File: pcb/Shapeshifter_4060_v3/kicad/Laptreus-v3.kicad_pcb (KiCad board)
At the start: 2 copper layers, 285 x 94.6 mm, 107 parts, among them SW1 TAB, SW10 O, SW11 P, SW12 BKSP, SW13 ESC, SW14 A, SW15 S, SW16 D, SW17 F/LOWER, SW18 G, SW19 H, SW2 Q, SW20 J/RAISE, SW21 K, SW22 L, SW23 ;, SW24 ", SW25 SHIFT, SW26 Z, SW27 X, SW28 C, SW29 V, SW3 W, SW30 B, SW31 N, SW32 M, SW33 ,, SW34 ., SW35 /, SW36 ENTER, SW37 HYPER, SW38 CTRL/GRV, SW39 ALT/TAB, SW4 E, SW40 CMD, SW41 SHIFT, SW42 BKSP/LIFT, SW43 ENTER/LIFT, SW44 SPACE, SW45 LEFT, SW46 DOWN, SW47 UP, SW48 RIGHT, SW5 R, SW6 T, SW7 Y, SW8 U, SW9 I

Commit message: Import footprints from other versions of the laptreus
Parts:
- BOARD1: footprint Shapeshifter 4060 Footprints:60_percent_plus_tofu_no_center_holes -> Kitsune-Footprints:60_percent_plus_tofu_no_center_holes
- D1, D10, D11, D12, D13, D14, D15, D16, D17, D18, D19, D2, D20, D21, D22, D23, D24, D25, D26, D27, D28, D29, D3, D30, D31, D32, D33, D34, D35, D36, D37, D38, D39, D4, D40, D41, D42, D43, D44, D45, D46, D47, D48, D5, D6, D7, D8, D9: footprint Shapeshifter 4060 Footprints:D_SOD-323_With_Test_Points -> Kitsune-Footprints:Diode-dual
- FID1, FID2, FID3, FID4: footprint Shapeshifter 4060 Footprints:FIDUCIAL -> Kitsune-Footprints:FIDUCIAL
- JP1, JP2, JP3: footprint Shapeshifter 4060 Footprints:1X01-CLEANBIG -> Kitsune-Footprints:1X01-CLEANBIG
- S9: footprint Shapeshifter 4060 Footprints:5mm_M2.5_Screw_Hole_Plated -> Kitsune-Footprints:5mm_M2.5_Screw_Hole_Plated
- SW1, SW10, SW11, SW12, SW13, SW14, SW15, SW16, SW17, SW18, SW19, SW2, SW20, SW21, SW22, SW23, SW24, SW25, SW26, SW27, SW28, SW29, SW3, SW30, SW31, SW32, SW33, SW34, SW35, SW36, SW37, SW38, SW39, SW4, SW40, SW41, SW42, SW43, SW44, SW45, SW46, SW47, SW48, SW5, SW6, SW7, SW8, SW9: footprint Shapeshifter 4060 Footprints:Kailh_Socket_With_Diode -> Kitsune-Footprints:Kailh_Socket_With_Diode_And_THT
- SW_POW_EN1, SW_POW_EN2: footprint Shapeshifter 4060 Footprints:EG1218 -> Kitsune-Footprints:EG1218
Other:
- board size 285 x 94.6 mm -> 285 x 95.1 mm
- board text added: "Shapeshifter 4060 v3.0"
- board text removed: "Shapeshifter 4060 v2.3"

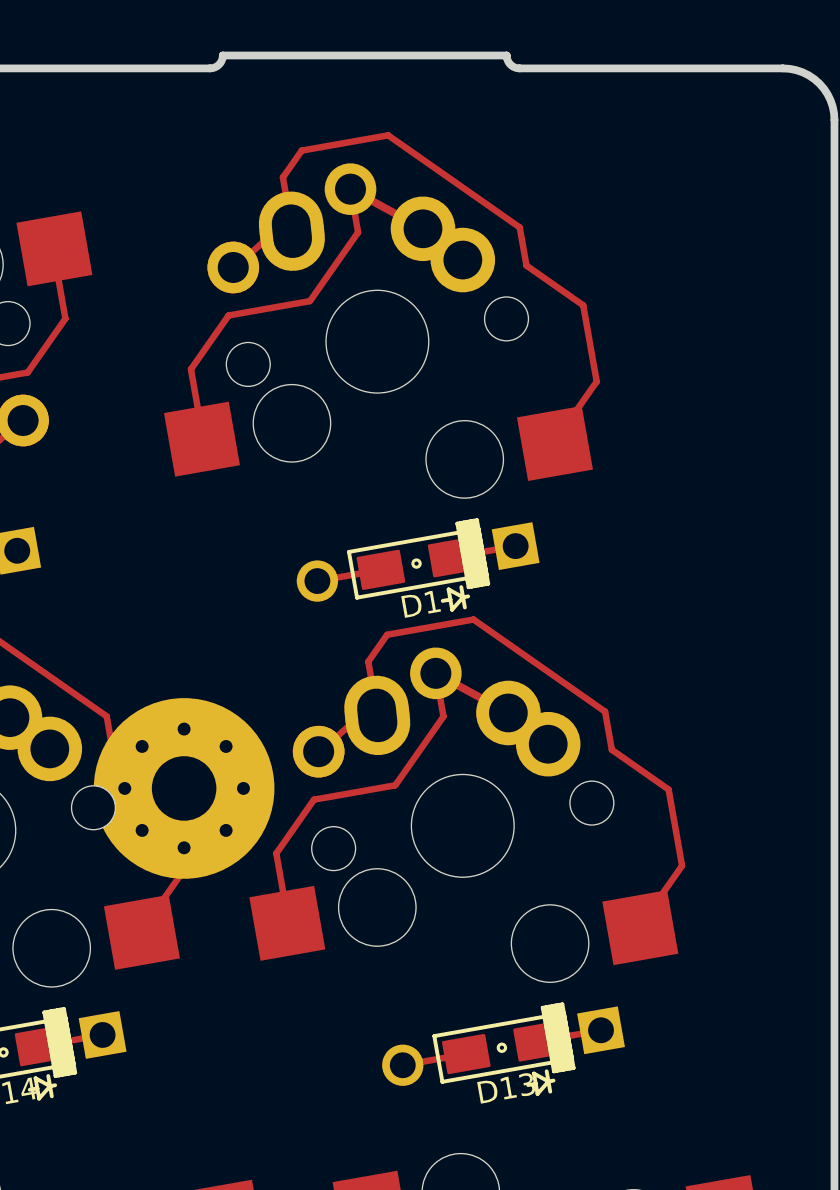
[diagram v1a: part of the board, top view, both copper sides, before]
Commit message: Update footprints for all objects on the PCB and annotate schema
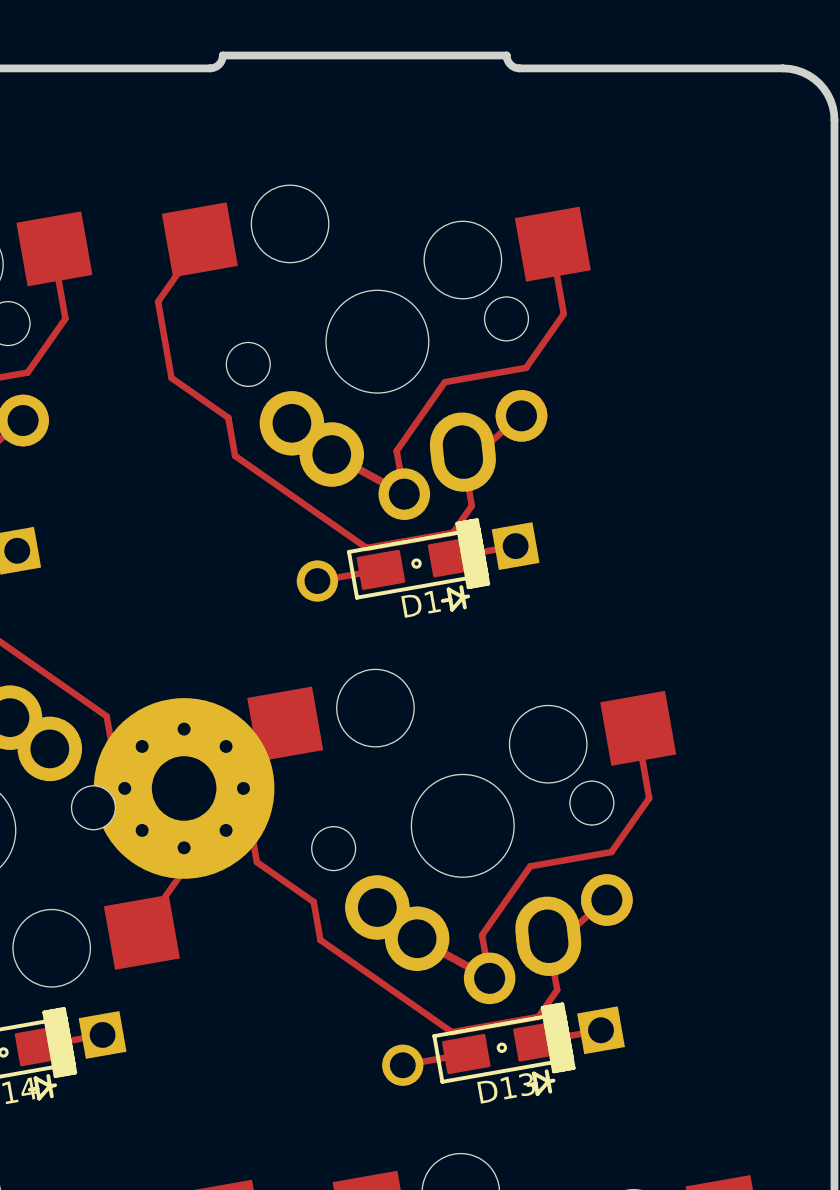
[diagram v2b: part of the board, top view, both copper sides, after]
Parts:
- turned SW1 to 10 degrees
- turned SW13 to 10 degrees

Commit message: Update diode positions on the pcb
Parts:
- moved D41 18.3 mm to (179.4, 125.8)
- moved D36 13.8 mm to (8.22, 85.6), turned to 80 degrees
- moved D43 11.5 mm to (122.7, 105.5), turned to 47.5 degrees
- moved D10 11.0 mm to (53.4, 48.9), turned to 80 degrees
- moved D11 11.0 mm to (34.1, 48.7), turned to 80 degrees
- moved D12 11.0 mm to (14.7, 48.5), turned to 80 degrees
- moved D19 11.0 mm to (106.3, 77.5), turned to 80 degrees
- moved D22 11.0 mm to (50.1, 67.6), turned to 80 degrees
- moved D33 11.0 mm to (66.1, 86.6), turned to 80 degrees
- moved D46 11.0 mm to (61.7, 111.6), turned to 80 degrees
- moved D7 11.0 mm to (109.7, 58.8), turned to 80 degrees
- moved D48 11.0 mm to (24.1, 105.0), turned to 80 degrees
- moved D34 11.0 mm to (46.8, 86.4), turned to 80 degrees
- moved D47 11.0 mm to (42.9, 108.3), turned to 80 degrees
- moved D20 11.0 mm to (87.6, 74.2), turned to 80 degrees
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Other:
- board text added: "4 diodes misplaced Diode labels are overlapping themselves Remove battery compartment Remove USB outdent (but leave the mark in case I want to cut that part out for a usb c port) Import pro micro footprint Add JST-SH connector"

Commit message: Finished moving Diodes around
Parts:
- SW1, SW10, SW11, SW12, SW15, SW16, SW17, SW18, SW19, SW2, SW20, SW21, SW22, SW25, SW26, SW27, SW28, SW29, SW3, SW30, SW31, SW32, SW33, SW34, SW35, SW37, SW38, SW39, SW4, SW40, SW41, SW42, SW43, SW44, SW45, SW46, SW47, SW48, SW5, SW6, SW7, SW8, SW9: footprint Kitsune-Footprints:Kailh_Socket_With_Diode_And_THT -> Kitsune-Footprints:Hybrid_Kailh_MX_Choc_Socket_Through_Hole_With_Diode
- SW13, SW14, SW23, SW24, SW36: footprint Kitsune-Footprints:Kailh_Socket_With_Diode_And_THT -> Kitsune-Footprints:Hybrid_Kailh_MX_Choc_Socket_Through_Hole_With_Diode_No_Diode_Trace
- moved D24 10.2 mm to (28.2, 74.5), turned to 80 degrees
- moved D14 9.05 mm to (266.9, 74.4), turned to 100 degrees
- moved D13 8.06 mm to (269.6, 74.0), turned to 100 degrees
- moved D23 2.63 mm to (34.9, 75.5), turned to 350 degrees

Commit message: added fids/jumpers to schematic, fixed wiring typo, added pro micro fo otprint
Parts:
- removed SW_POW_EN1, SW_POW_EN2: SW_SPDT, Kitsune-Footprints:EG1218
- added FID5: Fiducial, Kitsune-Footprints:FIDUCIAL, F.Cu at (287.5, 75.5)
- added FID6: Fiducial, Kitsune-Footprints:FIDUCIAL, B.Cu at (287.5, 75.5)
- added JP1: PINHD-1X1CB, Kitsune-Footprints:1X01-CLEANBIG, F.Cu at (127.6, 85.1)
- added U1: nice_nano, nice-nano-kicad:nice_nano, F.Cu at (147.7, 112.0)
- moved FID1 139.7 mm to (147.8, 129.9)
- moved FID2 139.7 mm to (147.8, 129.9)
- moved JP2 5.45 mm to (127.6, 82.5)
- moved JP3 3.83 mm to (127.6, 90.2)
- moved JP4 3.37 mm to (127.6, 87.6)
- renumbered JP1 to JP4
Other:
- board text added: "RX"
- board text added: "Remove battery compartment Remove USB outdent (but leave the mark in case I want to cut that part out for a usb c port) Import pro micro footprint Add JST-SH connector"
- board text added: "TX"
- board text removed: "4 diodes misplaced Diode labels are overlapping themselves Remove battery compartment Remove USB outdent (but leave the mark in case I want to cut that part out for a usb c port) Import pro micro footprint Add JST-SH connector"
- board text removed: "B7"

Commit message: Add nomask variant of nice nano, remove adhesives, add reset switch
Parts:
- removed S9: Tofu screw, Kitsune-Footprints:5mm_M2.5_Screw_Hole_Plated
- added SW_RESET_1: RESET, Kitsune-Footprints:SW_SPST_B3U-1000P, B.Cu at (147.8, 44.0)
- BOARD1: value BoardOutline -> Conn_01x01
- FID1, FID2, FID3, FID4, FID5, FID6: value Fiducial -> Conn_01x01
- JP1, JP2, JP3, JP4: value PINHD-1X1CB -> Conn_01x01
- SW13: footprint Kitsune-Footprints:Hybrid_Kailh_MX_Choc_Socket_Through_Hole_With_Diode_No_Diode_Trace -> Kitsune-Footprints:Hybrid_Kailh_MX_Choc_Socket_Through_Hole_With_Diode
- SW17: value F/LOWER -> F
- SW20: value J/RAISE -> J
- SW24: value " -> ENTER
- SW36: value ENTER -> SHIFT; footprint Kitsune-Footprints:Hybrid_Kailh_MX_Choc_Socket_Through_Hole_With_Diode_No_Diode_Trace -> Kitsune-Footprints:Hybrid_Kailh_MX_Choc_Socket_Through_Hole_With_Diode
- SW37: value HYPER -> CTRL/ESC
- SW38: value CTRL/GRV -> ALT/GRV
- SW39: value ALT/TAB -> CMD
- SW40: value CMD -> FN1
- SW42: value BKSP/LIFT -> BKSP
- SW43: value ENTER/LIFT -> ENTER
- U1: value nice_nano -> nice_nano_no_Bcu_mask; footprint nice-nano-kicad:nice_nano -> Kitsune-Footprints:nice_nano_no_Bcu_mask
- moved U1 27.3 mm to (147.8, 84.8)
- moved D14 10.3 mm to (256.8, 76.0), turned to 10 degrees
- moved D13 6.79 mm to (276.1, 75.8), turned to 10 degrees
- turned SW13 to 190 degrees
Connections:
- BOARD1 pad 1: (no net) -> GND
- D1 pad 1: (no net) -> Net-(D1-Pad1)
- D1 pad 2: (no net) -> /COL0
- D10 pad 1: (no net) -> Net-(D10-Pad1)
- D10 pad 2: (no net) -> /COL9
- D11 pad 1: (no net) -> Net-(D11-Pad1)
- D11 pad 2: (no net) -> /COL10
- D12 pad 1: (no net) -> Net-(D12-Pad1)
- D12 pad 2: (no net) -> /COL11
- D13 pad 1: (no net) -> Net-(D13-Pad1)
- D13 pad 2: (no net) -> /COL0
- D14 pad 1: (no net) -> Net-(D14-Pad1)
- D14 pad 2: (no net) -> /COL1
- D15 pad 1: (no net) -> Net-(D15-Pad1)
- D15 pad 2: (no net) -> /COL2
- D16 pad 1: (no net) -> Net-(D16-Pad1)
- D16 pad 2: (no net) -> /COL3
- D17 pad 1: (no net) -> Net-(D17-Pad1)
- D17 pad 2: (no net) -> /COL4
- D18 pad 1: (no net) -> Net-(D18-Pad1)
- D18 pad 2: (no net) -> /COL5
- D19 pad 1: (no net) -> Net-(D19-Pad1)
- D19 pad 2: (no net) -> /COL6
- D2 pad 1: (no net) -> Net-(D2-Pad1)
- D2 pad 2: (no net) -> /COL1
- D20 pad 1: (no net) -> Net-(D20-Pad1)
- D20 pad 2: (no net) -> /COL7
- D21 pad 1: (no net) -> Net-(D21-Pad1)
- D21 pad 2: (no net) -> /COL8
- D22 pad 1: (no net) -> Net-(D22-Pad1)
- D22 pad 2: (no net) -> /COL9
- D23 pad 1: (no net) -> Net-(D23-Pad1)
- D23 pad 2: (no net) -> /COL10
- D24 pad 1: (no net) -> Net-(D24-Pad1)
- D24 pad 2: (no net) -> /COL11
- D25 pad 1: (no net) -> Net-(D25-Pad1)
- D25 pad 2: (no net) -> /COL0
- D26 pad 1: (no net) -> Net-(D26-Pad1)
- D26 pad 2: (no net) -> /COL1
- D27 pad 1: (no net) -> Net-(D27-Pad1)
- D27 pad 2: (no net) -> /COL2
- D28 pad 1: (no net) -> Net-(D28-Pad1)
- D28 pad 2: (no net) -> /COL3
- D29 pad 1: (no net) -> Net-(D29-Pad1)
- D29 pad 2: (no net) -> /COL4
- D3 pad 1: (no net) -> Net-(D3-Pad1)
- D3 pad 2: (no net) -> /COL2
- D30 pad 1: (no net) -> Net-(D30-Pad1)
- D30 pad 2: (no net) -> /COL5
- D31 pad 1: (no net) -> Net-(D31-Pad1)
- D31 pad 2: (no net) -> /COL6
- D32 pad 1: (no net) -> Net-(D32-Pad1)
- D32 pad 2: (no net) -> /COL7
- D33 pad 1: (no net) -> Net-(D33-Pad1)
- D33 pad 2: (no net) -> /COL8
- D34 pad 1: (no net) -> Net-(D34-Pad1)
- D34 pad 2: (no net) -> /COL9
- D35 pad 1: (no net) -> Net-(D35-Pad1)
- D35 pad 2: (no net) -> /COL10
- D36 pad 1: (no net) -> Net-(D36-Pad1)
- D36 pad 2: (no net) -> /COL11
- D37 pad 1: (no net) -> Net-(D37-Pad1)
- D37 pad 2: (no net) -> /COL0
- D38 pad 1: (no net) -> Net-(D38-Pad1)
- D38 pad 2: (no net) -> /COL1
- D39 pad 1: (no net) -> Net-(D39-Pad1)
- D39 pad 2: (no net) -> /COL2
- D4 pad 1: (no net) -> Net-(D4-Pad1)
- D4 pad 2: (no net) -> /COL3
- D40 pad 1: (no net) -> Net-(D40-Pad1)
- D40 pad 2: (no net) -> /COL3
- D41 pad 1: (no net) -> Net-(D41-Pad1)
- D41 pad 2: (no net) -> /COL4
- D42 pad 1: (no net) -> Net-(D42-Pad1)
- D42 pad 2: (no net) -> /COL5
- D43 pad 1: (no net) -> Net-(D43-Pad1)
- D43 pad 2: (no net) -> /COL6
- D44 pad 1: (no net) -> Net-(D44-Pad1)
- D44 pad 2: (no net) -> /COL7
- D45 pad 1: (no net) -> Net-(D45-Pad1)
- D45 pad 2: (no net) -> /COL8
- D46 pad 1: (no net) -> Net-(D46-Pad1)
- D46 pad 2: (no net) -> /COL9
- D47 pad 1: (no net) -> Net-(D47-Pad1)
- D47 pad 2: (no net) -> /COL10
- D48 pad 1: (no net) -> Net-(D48-Pad1)
- D48 pad 2: (no net) -> /COL11
- D5 pad 1: (no net) -> Net-(D5-Pad1)
- D5 pad 2: (no net) -> /COL4
- D6 pad 1: (no net) -> Net-(D6-Pad1)
- D6 pad 2: (no net) -> /COL5
- D7 pad 1: (no net) -> Net-(D7-Pad1)
- D7 pad 2: (no net) -> /COL6
- D8 pad 1: (no net) -> Net-(D8-Pad1)
- D8 pad 2: (no net) -> /COL7
- D9 pad 1: (no net) -> Net-(D9-Pad1)
- D9 pad 2: (no net) -> /COL8
- FID1 pad 1: (no net) -> GND
- FID2 pad 1: (no net) -> GND
- FID3 pad 1: (no net) -> GND
- FID4 pad 1: (no net) -> GND
- FID5 pad 1: (no net) -> GND
- FID6 pad 1: (no net) -> GND
- JP1 pad 1: (no net) -> /TX
- JP2 pad 1: (no net) -> GND
- JP3 pad 1: (no net) -> /VCC
- JP4 pad 1: (no net) -> /RX
- SW1 pad 1: (no net) -> /ROW0
- SW1 pad 2: (no net) -> Net-(D1-Pad1)
- SW10 pad 1: (no net) -> /ROW0
- SW10 pad 2: (no net) -> Net-(D10-Pad1)
- SW11 pad 1: (no net) -> /ROW0
- SW11 pad 2: (no net) -> Net-(D11-Pad1)
- SW12 pad 1: (no net) -> /ROW0
- SW12 pad 2: (no net) -> Net-(D12-Pad1)
- SW13 pad 1: (no net) -> /COL3
- SW13 pad 2: (no net) -> Net-(D13-Pad1)
- SW14 pad 1: (no net) -> /COL3
- SW14 pad 2: (no net) -> Net-(D14-Pad1)
- SW15 pad 1: (no net) -> /COL3
- SW15 pad 2: (no net) -> Net-(D15-Pad1)
- SW16 pad 1: (no net) -> /COL3
- SW16 pad 2: (no net) -> Net-(D16-Pad1)
- SW17 pad 1: (no net) -> /COL3
- SW17 pad 2: (no net) -> Net-(D17-Pad1)
- SW18 pad 1: (no net) -> /COL3
- SW18 pad 2: (no net) -> Net-(D18-Pad1)
- SW19 pad 1: (no net) -> /COL3
- SW19 pad 2: (no net) -> Net-(D19-Pad1)
- SW2 pad 1: (no net) -> /ROW0
- SW2 pad 2: (no net) -> Net-(D2-Pad1)
- SW20 pad 1: (no net) -> /COL3
- SW20 pad 2: (no net) -> Net-(D20-Pad1)
- SW21 pad 1: (no net) -> /COL3
- SW21 pad 2: (no net) -> Net-(D21-Pad1)
- SW22 pad 1: (no net) -> /COL3
- SW22 pad 2: (no net) -> Net-(D22-Pad1)
- SW23 pad 1: (no net) -> /COL3
- SW23 pad 2: (no net) -> Net-(D23-Pad1)
- SW24 pad 1: (no net) -> /COL3
- SW24 pad 2: (no net) -> Net-(D24-Pad1)
- SW25 pad 1: (no net) -> /ROW2
- SW25 pad 2: (no net) -> Net-(D25-Pad1)
- SW26 pad 1: (no net) -> /ROW2
- SW26 pad 2: (no net) -> Net-(D26-Pad1)
- SW27 pad 1: (no net) -> /ROW2
- SW27 pad 2: (no net) -> Net-(D27-Pad1)
- SW28 pad 1: (no net) -> /ROW2
- SW28 pad 2: (no net) -> Net-(D28-Pad1)
- SW29 pad 1: (no net) -> /ROW2
- SW29 pad 2: (no net) -> Net-(D29-Pad1)
- SW3 pad 1: (no net) -> /ROW0
- SW3 pad 2: (no net) -> Net-(D3-Pad1)
- SW30 pad 1: (no net) -> /ROW2
- SW30 pad 2: (no net) -> Net-(D30-Pad1)
- SW31 pad 1: (no net) -> /ROW2
- SW31 pad 2: (no net) -> Net-(D31-Pad1)
- SW32 pad 1: (no net) -> /ROW2
- SW32 pad 2: (no net) -> Net-(D32-Pad1)
- SW33 pad 1: (no net) -> /ROW2
- SW33 pad 2: (no net) -> Net-(D33-Pad1)
- SW34 pad 1: (no net) -> /ROW2
- SW34 pad 2: (no net) -> Net-(D34-Pad1)
- SW35 pad 1: (no net) -> /ROW2
- SW35 pad 2: (no net) -> Net-(D35-Pad1)
- SW36 pad 1: (no net) -> /ROW2
- SW36 pad 2: (no net) -> Net-(D36-Pad1)
- SW37 pad 1: (no net) -> /ROW3
- SW37 pad 2: (no net) -> Net-(D37-Pad1)
- SW38 pad 1: (no net) -> /ROW3
- SW38 pad 2: (no net) -> Net-(D38-Pad1)
- SW39 pad 1: (no net) -> /ROW3
- SW39 pad 2: (no net) -> Net-(D39-Pad1)
- SW4 pad 1: (no net) -> /ROW0
- SW4 pad 2: (no net) -> Net-(D4-Pad1)
- SW40 pad 1: (no net) -> /ROW3
- SW40 pad 2: (no net) -> Net-(D40-Pad1)
- SW41 pad 1: (no net) -> /ROW3
- SW41 pad 2: (no net) -> Net-(D41-Pad1)
- SW42 pad 1: (no net) -> /ROW3
- SW42 pad 2: (no net) -> Net-(D42-Pad1)
- SW43 pad 1: (no net) -> /ROW3
- SW43 pad 2: (no net) -> Net-(D43-Pad1)
- SW44 pad 1: (no net) -> /ROW3
- SW44 pad 2: (no net) -> Net-(D44-Pad1)
- SW45 pad 1: (no net) -> /ROW3
- SW45 pad 2: (no net) -> Net-(D45-Pad1)
- SW46 pad 1: (no net) -> /ROW3
- SW46 pad 2: (no net) -> Net-(D46-Pad1)
- SW47 pad 1: (no net) -> /ROW3
- SW47 pad 2: (no net) -> Net-(D47-Pad1)
- SW48 pad 1: (no net) -> /ROW3
- SW48 pad 2: (no net) -> Net-(D48-Pad1)
- SW5 pad 1: (no net) -> /ROW0
- SW5 pad 2: (no net) -> Net-(D5-Pad1)
- SW6 pad 1: (no net) -> /ROW0
- SW6 pad 2: (no net) -> Net-(D6-Pad1)
- SW7 pad 1: (no net) -> /ROW0
- SW7 pad 2: (no net) -> Net-(D7-Pad1)
- SW8 pad 1: (no net) -> /ROW0
- SW8 pad 2: (no net) -> Net-(D8-Pad1)
- SW9 pad 1: (no net) -> /ROW0
- SW9 pad 2: (no net) -> Net-(D9-Pad1)
- U1 pad 1: (no net) -> /TX
- U1 pad 10: (no net) -> /COL5
- U1 pad 11: (no net) -> /COL6
- U1 pad 12: (no net) -> /COL7
- U1 pad 13: (no net) -> /COL8
- U1 pad 14: (no net) -> /COL9
- U1 pad 15: (no net) -> /COL10
- U1 pad 16: (no net) -> /COL11
- U1 pad 17: (no net) -> /ROW3
- U1 pad 18: (no net) -> /ROW2
- U1 pad 19: (no net) -> /COL3
- U1 pad 2: (no net) -> /RX
- U1 pad 20: (no net) -> /ROW0
- U1 pad 21: (no net) -> /VCC
- U1 pad 22: (no net) -> /RESET
- U1 pad 23: (no net) -> GND
- U1 pad 3: (no net) -> GND
- U1 pad 4: (no net) -> GND
- U1 pad 5: (no net) -> /COL0
- U1 pad 6: (no net) -> /COL1
- U1 pad 7: (no net) -> /COL2
- U1 pad 8: (no net) -> /COL3
- U1 pad 9: (no net) -> /COL4

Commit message: all components wired up!
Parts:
- U1: value nice_nano_no_Bcu_mask -> nice_nano
- moved JP1 9.17 mm to (127.6, 75.9)
- moved JP4 8.71 mm to (127.6, 78.9)
- moved JP3 5.25 mm to (127.6, 84.9)
- moved D17 1.10 mm to (191.8, 76.0)
- moved D20 1.10 mm to (87.4, 73.1)
- moved D10 1.10 mm to (53.2, 47.8)
- moved SW18 1.10 mm to (180.8, 76.6)
- moved SW41 1.10 mm to (184.6, 118.6)
- moved SW12 1.10 mm to (22.8, 47.5)
- moved D33 1.10 mm to (65.9, 85.5)
- moved SW1 1.10 mm to (272.4, 47.6)
- moved SW10 1.10 mm to (61.4, 47.9)
- moved D15 1.10 mm to (229.3, 69.4)
- moved D19 1.10 mm to (106.2, 76.5)
- moved SW35 1.10 mm to (35.5, 85.3)
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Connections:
- SW13 pad 1: /COL3 -> /ROW1
- SW14 pad 1: /COL3 -> /ROW1
- SW15 pad 1: /COL3 -> /ROW1
- SW16 pad 1: /COL3 -> /ROW1
- SW17 pad 1: /COL3 -> /ROW1
- SW18 pad 1: /COL3 -> /ROW1
- SW19 pad 1: /COL3 -> /ROW1
- SW20 pad 1: /COL3 -> /ROW1
- SW21 pad 1: /COL3 -> /ROW1
- SW22 pad 1: /COL3 -> /ROW1
- SW23 pad 1: /COL3 -> /ROW1
- SW24 pad 1: /COL3 -> /ROW1
- U1 pad 10: /COL5 -> /COL8
- U1 pad 11: /COL6 -> /COL7
- U1 pad 12: /COL7 -> /COL6
- U1 pad 13: /COL8 -> /COL5
- U1 pad 14: /COL9 -> /COL4
- U1 pad 15: /COL10 -> /COL3
- U1 pad 16: /COL11 -> /COL2
- U1 pad 19: /COL3 -> /ROW1
- U1 pad 24: (no net) -> Net-(U1-Pad24)
- U1 pad 31: (no net) -> Net-(U1-Pad31)
- U1 pad 32: (no net) -> Net-(U1-Pad32)
- U1 pad 33: (no net) -> Net-(U1-Pad33)
- U1 pad 5: /COL0 -> /COL1
- U1 pad 6: /COL1 -> /COL0
- U1 pad 7: /COL2 -> /COL11
- U1 pad 8: /COL3 -> /COL10
- U1 pad 9: /COL4 -> /COL9
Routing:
- net /ROW0: track 0.00 -> 354.5 mm
- net /ROW1: track 0.00 -> 336.3 mm
- net /ROW2: track 0.00 -> 323.3 mm
- net /ROW3: track 0.00 -> 308.8 mm
- net /COL11: track 0.00 -> 265.7 mm
- net /COL0: track 0.00 -> 235.4 mm
- net /COL10: track 0.00 -> 224.5 mm
- net /COL1: track 0.00 -> 216.2 mm
- net /COL9: track 0.00 -> 197.5 mm
- net /COL2: track 0.00 -> 184.7 mm
- net /COL8: track 0.00 -> 176.1 mm
- net /COL3: track 0.00 -> 164.1 mm
- net /COL7: track 0.00 -> 149.3 mm
- net /COL4: track 0.00 -> 139.2 mm
- net /COL6: track 0.00 -> 131.1 mm
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- added copper zone on F.Cu, net GND
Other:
- board text added: "Remove battery compartment Remove USB outdent (but leave the mark in case I want to cut that part out for a usb c port) 1. Show all layers 2. Select all and rotate 3. Hide Dwgs.User and set grid origin to the yellow cross 4. Set the grid back to 0.1mm 5. Do some work"
- board text removed: "Remove battery compartment Remove USB outdent (but leave the mark in case I want to cut that part out for a usb c port) Import pro micro footprint Add JST-SH connector"

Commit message: Move reminders to a readme
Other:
- board size 285 x 95.1 mm -> 285 x 94.6 mm
- board text added: "Kitsune Keyboards Shapeshifter 4060 v3.0"
- board text removed: "Remove battery compartment Remove USB outdent (but leave the mark in case I want to cut that part out for a usb c port) 1. Show all layers 2. Select all and rotate 3. Hide Dwgs.User and set grid origin to the yellow cross 4. Set the grid back to 0.1mm 5. Do some work"
- board text removed: "Shapeshifter 4060 v3.0"
